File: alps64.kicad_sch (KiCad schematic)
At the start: 15 parts, among them J1 USB_mini_micro_B, SW100 SW_PUSH, U1 32U2, X1 XTAL_GND

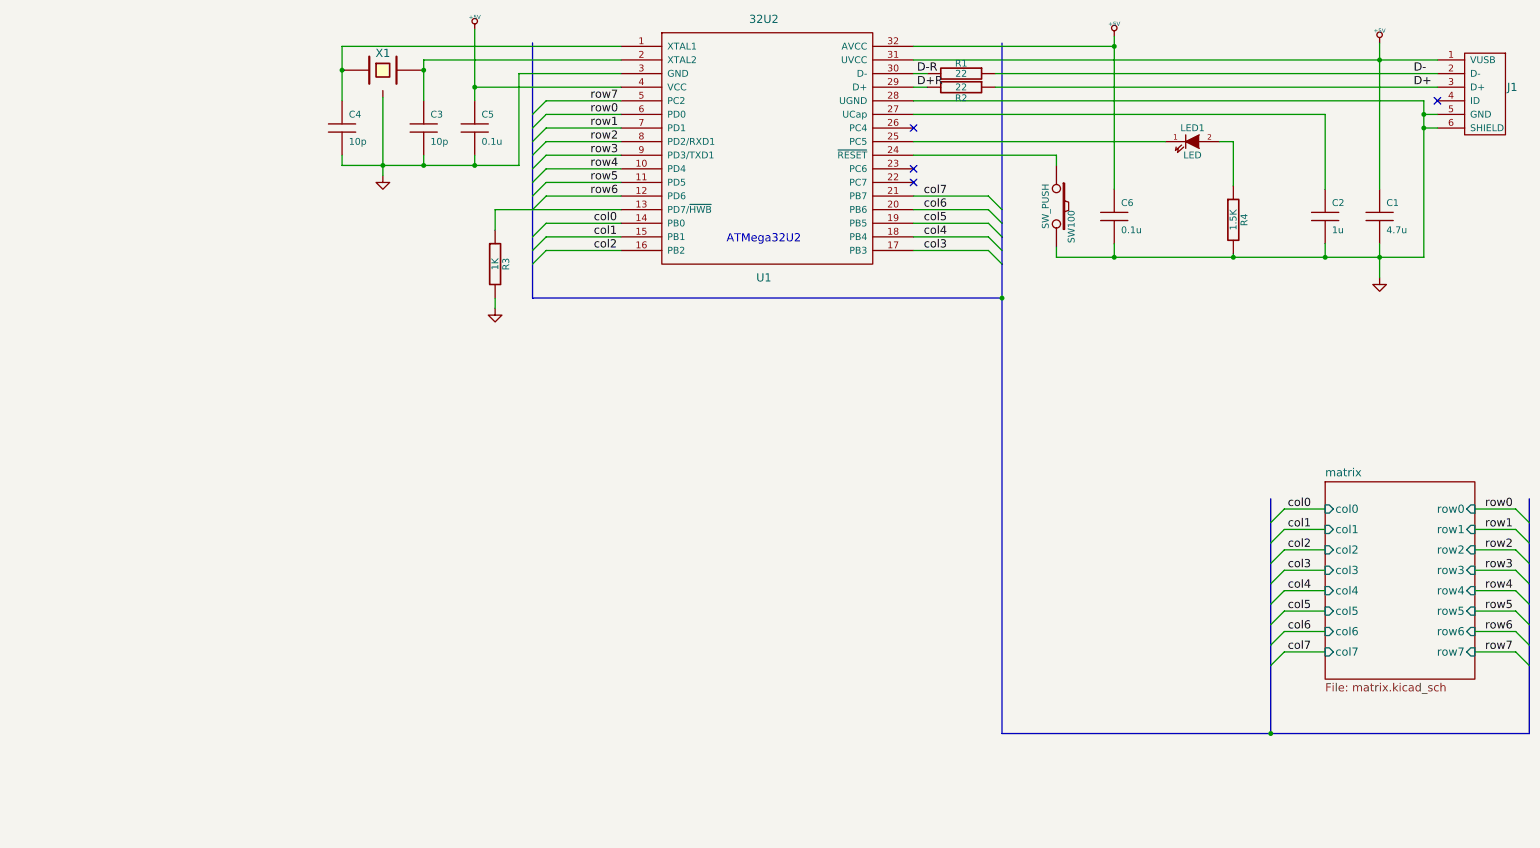
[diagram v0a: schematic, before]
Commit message: Update footprints
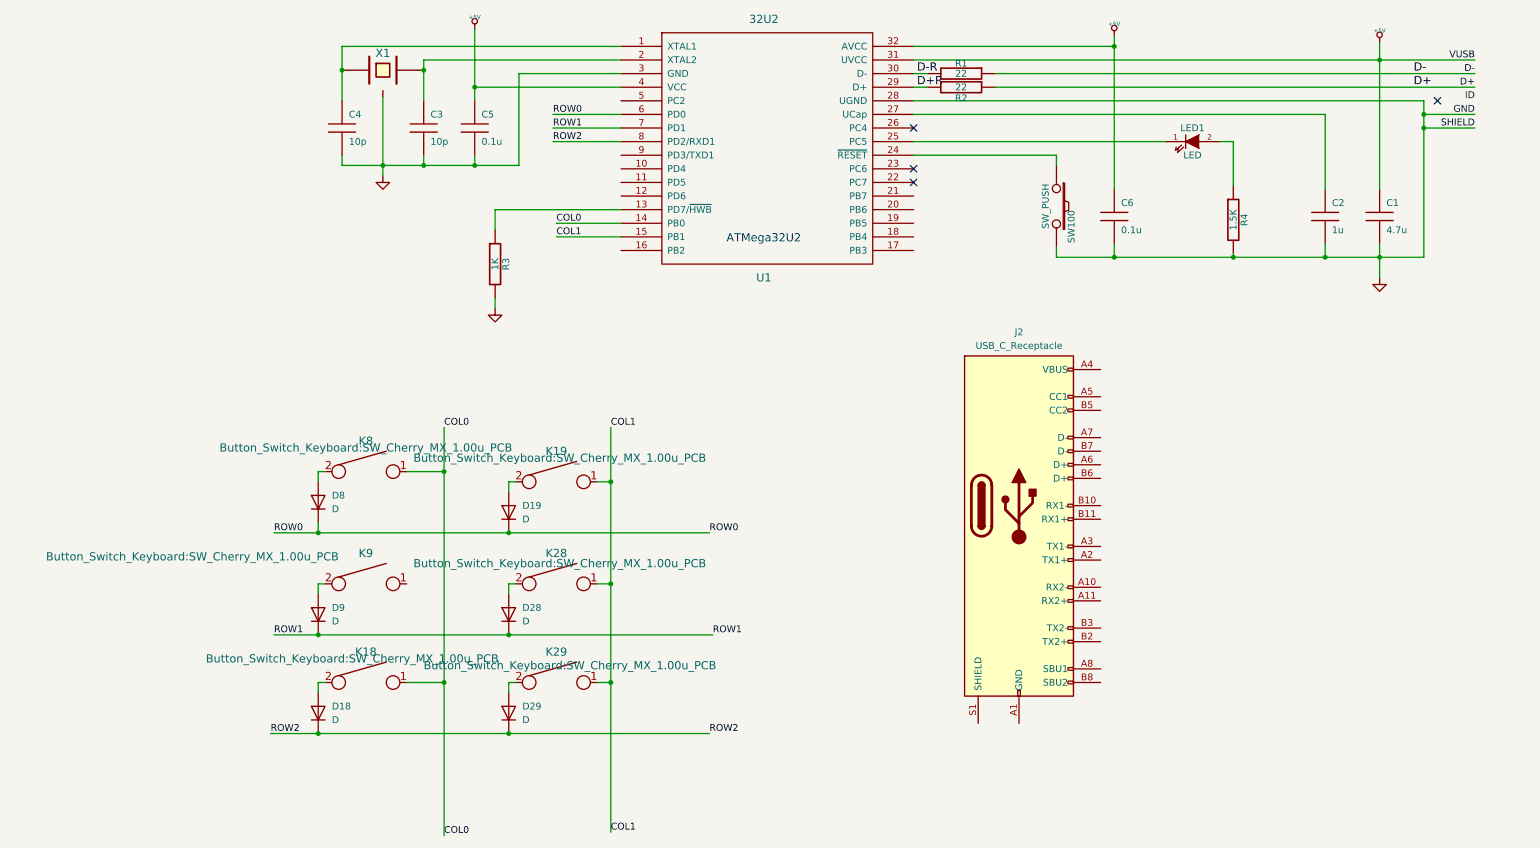
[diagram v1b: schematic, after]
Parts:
- removed J1: USB_mini_micro_B, keyboard_parts:USB_miniB_hirose_th_reflow, symbol alps64-rescue:USB_mini_micro_B-keyboard_parts
- added D18, D19, D28, D29, D8, D9: D, Diode_SMD:D_SOD-323, symbol Device:D
- added J2: USB_C_Receptacle, Connector_USB:USB_C_Receptacle_HCTL_HC-TYPE-C-16P-01A, symbol Connector:USB_C_Receptacle
- added K18, K19, K28, K29, K8, K9: keyboard_parts:KEYSW, Button_Switch_Keyboard:SW_Cherry_MX_1.00u_PCB, symbol alps64-rescue:KEYSW-keyboard_parts
- C1: footprint keyboard_parts:C_3216 -> Capacitor_SMD:C_0603_1608Metric
- C2, C3, C4: footprint keyboard_parts:C_1608 -> Capacitor_SMD:C_0603_1608Metric
- C5, C6: footprint keyboard_parts:C_1608 -> Capacitor_THT:C_Disc_D3.0mm_W1.6mm_P2.50mm
- LED1: footprint keyboard_parts:LED_2012_HSOL -> LED_THT:LED_D1.8mm_W3.3mm_H2.4mm
- R1, R2, R3, R4: footprint keyboard_parts:R_1608 -> Resistor_THT:R_Axial_DIN0204_L3.6mm_D1.6mm_P7.62mm_Horizontal
- SW100: footprint keyboard_parts:SW_ALPS_SKRP -> Button_Switch_THT:SW_PUSH_6mm
- U1: footprint keyboard_parts:QFP32_reflow -> Package_QFP:TQFP-32_7x7mm_P0.8mm
- X1: value XTAL_GND -> 16MHz; footprint (none) -> Crystal:Crystal_SMD_3225-4Pin_3.2x2.5mm
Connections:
- net col0 renamed COL0
- net COL0: now also K18.1, K8.1
- net col1 renamed COL1
- net COL1: now also K19.1, K28.1, K29.1
- net col2: no longer names the net of U1.16 (PB2)
- net col3: no longer names the net of U1.17 (PB3)
- net col4: no longer names the net of U1.18 (PB4)
- net col5: no longer names the net of U1.19 (PB5)
- net col6: no longer names the net of U1.20 (PB6)
- net col7: no longer names the net of U1.21 (PB7)
- net row0 renamed ROW0
- net ROW0: now also D19.1 (K), D8.1 (K)
- net row1 renamed ROW1
- net ROW1: now also D28.1 (K), D9.1 (K)
- net row2 renamed ROW2
- net ROW2: now also D18.1 (K), D29.1 (K)
- net row3: no longer names the net of U1.9 (PD3/TXD1)
- net row4: no longer names the net of U1.10 (PD4)
- net row5: no longer names the net of U1.11 (PD5)
- net row6: no longer names the net of U1.12 (PD6)
- net row7: no longer names the net of U1.5 (PC2)
- new net: D9.2 (A), K9.2
- new net: D28.2 (A), K28.2
- new net: D19.2 (A), K19.2
- new net: D8.2 (A), K8.2
- new net: D18.2 (A), K18.2
- new net: D29.2 (A), K29.2
- new net: J2.A1 (GND), J2.A12 (GND), J2.B1 (GND), J2.B12 (GND)
- new net: J2.A4 (VBUS), J2.A9 (VBUS), J2.B4 (VBUS), J2.B9 (VBUS)
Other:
- removed sheet matrix

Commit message: Update wiring
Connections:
- net D+: now also J2.A6 (D+), J2.B6 (D+)
- net D-: now also J2.A7 (D-), J2.B7 (D-)
- net GND: now also J2.A1 (GND), J2.A12 (GND), J2.B1 (GND), J2.B12 (GND)
- net VBUS: now reaches J2.A4 (VBUS), J2.A9 (VBUS), J2.B4 (VBUS), J2.B9 (VBUS)
- net SHILED: now reaches J2.S1 (SHIELD)
- no-connect marks 4 -> 14
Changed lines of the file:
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@@
   (junction (at 85.09 142.875) (diameter 0) (color 0 0 0 0)
   )
+  (no_connect (at 195.58 121.285))
   (no_connect (at 160.655 48.26))
+  (no_connect (at 195.58 118.745))
+  (no_connect (at 195.58 133.985))
+  (no_connect (at 195.58 136.525))
+  (no_connect (at 195.58 128.905))
   (no_connect (at 160.655 58.42))
+  (no_connect (at 195.58 151.765))
+  (no_connect (at 195.58 100.965))
+  (no_connect (at 195.58 126.365))
   (no_connect (at 160.655 55.88))
   (no_connect (at 258.445 43.18))
+  (no_connect (at 195.58 149.225))
+  (no_connect (at 195.58 98.425))
   (wire (pts (xy 85.09 133.35) (xy 85.09 135.255))
     (stroke (width 0) (type default))
@@
     (stroke (width 0) (type default))
   )
+  (wire (pts (xy 195.58 106.045) (xy 203.2 106.045))
+    (stroke (width 0) (type default))
+  )
   (wire (pts (xy 73.025 112.395) (xy 73.025 151.765))
     (stroke (width 0) (type default))
@@
     (stroke (width 0) (type default))
   )
+  (wire (pts (xy 172.72 159.385) (xy 172.72 166.37))
+    (stroke (width 0) (type default))
+  )
   (wire (pts (xy 41.275 123.825) (xy 49.53 123.825))
     (stroke (width 0) (type default))
@@
     (stroke (width 0) (type default))
   )
+  (wire (pts (xy 195.58 93.345) (xy 203.2 93.345))
+    (stroke (width 0) (type default))
+  )
+  (wire (pts (xy 195.58 108.585) (xy 203.2 108.585))
+    (stroke (width 0) (type default))
+  )
   (wire (pts (xy 86.995 38.1) (xy 86.995 55.245))
     (stroke (width 0) (type default))
@@
     (stroke (width 0) (type default))
   )
+  (wire (pts (xy 195.58 111.125) (xy 203.2 111.125))
+    (stroke (width 0) (type default))
+  )
   (wire (pts (xy 217.805 50.8) (xy 220.345 50.8))
     (stroke (width 0) (type default))
@@
   )
   (wire (pts (xy 85.09 114.3) (xy 85.09 116.205))
+    (stroke (width 0) (type default))
+  )
+  (wire (pts (xy 180.34 159.385) (xy 180.34 163.83))
+    (stroke (width 0) (type default))
+  )
+  (wire (pts (xy 195.58 113.665) (xy 203.2 113.665))
     (stroke (width 0) (type default))
   )
@@
     (effects (font (size 1.524 1.524)) (justify left bottom))
   )
+  (label "D-" (at 203.2 106.045 180) (fields_autoplaced)
+    (effects (font (size 1.27 1.27)) (justify right bottom))
+  )
   (label "ROW0" (at 41.275 123.825 0) (fields_autoplaced)
     (effects (font (size 1.27 1.27)) (justify left bottom))
@@
   )
   (label "ROW1" (at 41.275 142.875 0) (fields_autoplaced)
+    (effects (font (size 1.27 1.27)) (justify left bottom))
+  )
+  (label "GND" (at 180.34 163.83 90) (fields_autoplaced)
     (effects (font (size 1.27 1.27)) (justify left bottom))
   )
@@
     (effects (font (size 1.27 1.27)) (justify left bottom))
   )
+  (label "D-" (at 203.2 108.585 180) (fields_autoplaced)
+    (effects (font (size 1.27 1.27)) (justify right bottom))
+  )
   (label "ROW2" (at 93.345 50.8 0) (fields_autoplaced)
     (effects (font (size 1.27 1.27)) (justify left bottom))
@@
     (effects (font (size 1.27 1.27)) (justify left bottom))
   )
+  (label "D+" (at 203.2 111.125 180) (fields_autoplaced)
+    (effects (font (size 1.27 1.27)) (justify right bottom))
+  )
   (label "ID" (at 265.43 43.18 180) (fields_autoplaced)
     (effects (font (size 1.27 1.27)) (justify right bottom))
@@
     (effects (font (size 1.524 1.524)) (justify left bottom))
   )
+  (label "D+" (at 203.2 113.665 180) (fields_autoplaced)
+    (effects (font (size 1.27 1.27)) (justify right bottom))
+  )
+  (label "VBUS" (at 203.2 93.345 180) (fields_autoplaced)
+    (effects (font (size 1.27 1.27)) (justify right bottom))
+  )
+  (label "SHILED" (at 172.72 166.37 90) (fields_autoplaced)
+    (effects (font (size 1.27 1.27)) (justify left bottom))
+  )
   (symbol (lib_id "alps64-rescue:ATMEGA32U2-keyboard_parts") (at 132.715 52.07 0) (unit 1)
